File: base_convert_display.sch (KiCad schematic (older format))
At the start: 30 parts, among them Q10 Q_PNP_BEC, Q11 Q_PNP_BEC, Q12 Q_PNP_BEC, Q13 Q_PNP_BEC, Q14 Q_PNP_BEC, Q15 Q_PNP_BEC, Q16 Q_PNP_BEC, Q17 Q_PNP_BEC, Q18 Q_PNP_BEC, Q19 Q_PNP_BEC, Q20 Q_NPN_BEC, Q21 Q_NPN_BEC, Q22 Q_NPN_BEC, Q23 Q_NPN_BEC, Q24 Q_NPN_BEC, Q25 Q_NPN_BEC, Q26 Q_NPN_BEC, Q27 Q_NPN_BEC

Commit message: update RN part numbers
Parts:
- RN10, RN4, RN5, RN6, RN9: Description RES ARRAY 4 RES 4.7K OHM 1206 -> RES ARRAY 4 RES 5.6K OHM 2012; Manufacture Stackpole Electronics Inc. -> Rohm Semiconductor; Mfg Part Number RAVF164DJT4K70 -> MNR34J5ABJ562; Package 1206 -> 2012
- RN7, RN8: Mfg Part Number MNR14ERAPJ151 -> MNR34J5ABJ151; Package 1206 -> 2012
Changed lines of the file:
@@
 F 2 "Resistors_SMD:R_Array_Convex_4x1206" V 1425 1150 50  0001 C CNN
 F 3 "https://www.seielect.com/Catalog/SEI-RAVF.pdf" H 1150 1150 50  0001 C CNN
-F 4 "Stackpole Electronics Inc." H 1150 1150 60  0001 C CNN "Manufacture"
-F 5 "RAVF164DJT4K70" H 1150 1150 60  0001 C CNN "Mfg Part Number"
-F 6 "1206" H 1150 1150 60  0001 C CNN "Package"
-F 7 "RES ARRAY 4 RES 4.7K OHM 1206" H 1150 1150 60  0001 C CNN "Description"
+F 4 "Rohm Semiconductor" H 1150 1150 60  0001 C CNN "Manufacture"
+F 5 "MNR34J5ABJ562" H 1150 1150 60  0001 C CNN "Mfg Part Number"
+F 6 "2012" H 1150 1150 60  0001 C CNN "Package"
+F 7 "RES ARRAY 4 RES 5.6K OHM 2012" H 1150 1150 60  0001 C CNN "Description"
 	1    1150 1150
 	0    1    1    0
@@
 F 3 "http://rohmfs.rohm.com/en/products/databook/datasheet/passive/resistor/chip_resistor_network/mnr_g.pdf" H 8200 1000 50  0001 C CNN
 F 4 "Rohm Semiconductor" H 8200 1000 60  0001 C CNN "Manufacture"
-F 5 "MNR14ERAPJ151" H 8200 1000 60  0001 C CNN "Mfg Part Number"
-F 6 "1206" H 8200 1000 60  0001 C CNN "Package"
+F 5 "MNR34J5ABJ151" H 8200 1000 60  0001 C CNN "Mfg Part Number"
+F 6 "2012" H 8200 1000 60  0001 C CNN "Package"
 F 7 "RES ARRAY 4 RES 150 OHM 1206" H 8200 1000 60  0001 C CNN "Description"
 	1    8200 1000
@@
 F 2 "Resistors_SMD:R_Array_Convex_4x1206" V 1425 3950 50  0001 C CNN
 F 3 "https://www.seielect.com/Catalog/SEI-RAVF.pdf" H 1150 3950 50  0001 C CNN
-F 4 "Stackpole Electronics Inc." H 1150 3950 60  0001 C CNN "Manufacture"
-F 5 "RAVF164DJT4K70" H 1150 3950 60  0001 C CNN "Mfg Part Number"
-F 6 "1206" H 1150 3950 60  0001 C CNN "Package"
-F 7 "RES ARRAY 4 RES 4.7K OHM 1206" H 1150 3950 60  0001 C CNN "Description"
+F 4 "Rohm Semiconductor" H 1150 3950 60  0001 C CNN "Manufacture"
+F 5 "MNR34J5ABJ562" H 1150 3950 60  0001 C CNN "Mfg Part Number"
+F 6 "2012" H 1150 3950 60  0001 C CNN "Package"
+F 7 "RES ARRAY 4 RES 5.6K OHM 2012" H 1150 3950 60  0001 C CNN "Description"
 	1    1150 3950
 	0    1    1    0
@@
 F 2 "Resistors_SMD:R_Array_Convex_4x1206" V 1425 6750 50  0001 C CNN
 F 3 "https://www.seielect.com/Catalog/SEI-RAVF.pdf" H 1150 6750 50  0001 C CNN
-F 4 "Stackpole Electronics Inc." H 1150 6750 60  0001 C CNN "Manufacture"
-F 5 "RAVF164DJT4K70" H 1150 6750 60  0001 C CNN "Mfg Part Number"
-F 6 "1206" H 1150 6750 60  0001 C CNN "Package"
-F 7 "RES ARRAY 4 RES 4.7K OHM 1206" H 1150 6750 60  0001 C CNN "Description"
+F 4 "Rohm Semiconductor" H 1150 6750 60  0001 C CNN "Manufacture"
+F 5 "MNR34J5ABJ562" H 1150 6750 60  0001 C CNN "Mfg Part Number"
+F 6 "2012" H 1150 6750 60  0001 C CNN "Package"
+F 7 "RES ARRAY 4 RES 5.6K OHM 2012" H 1150 6750 60  0001 C CNN "Description"
 	1    1150 6750
 	0    1    1    0
@@
 F 3 "http://rohmfs.rohm.com/en/products/databook/datasheet/passive/resistor/chip_resistor_network/mnr_g.pdf" H 8200 4200 50  0001 C CNN
 F 4 "Rohm Semiconductor" H 8200 4200 60  0001 C CNN "Manufacture"
-F 5 "MNR14ERAPJ151" H 8200 4200 60  0001 C CNN "Mfg Part Number"
-F 6 "1206" H 8200 4200 60  0001 C CNN "Package"
+F 5 "MNR34J5ABJ151" H 8200 4200 60  0001 C CNN "Mfg Part Number"
+F 6 "2012" H 8200 4200 60  0001 C CNN "Package"
 F 7 "RES ARRAY 4 RES 150 OHM 1206" H 8200 4200 60  0001 C CNN "Description"
 	1    8200 4200
@@
 F 2 "Resistors_SMD:R_Array_Convex_4x1206" V 10125 1200 50  0001 C CNN
 F 3 "https://www.seielect.com/Catalog/SEI-RAVF.pdf" H 9850 1200 50  0001 C CNN
-F 4 "Stackpole Electronics Inc." H 9850 1200 60  0001 C CNN "Manufacture"
-F 5 "RAVF164DJT4K70" H 9850 1200 60  0001 C CNN "Mfg Part Number"
-F 6 "1206" H 9850 1200 60  0001 C CNN "Package"
-F 7 "RES ARRAY 4 RES 4.7K OHM 1206" H 9850 1200 60  0001 C CNN "Description"
+F 4 "Rohm Semiconductor" H 9850 1200 60  0001 C CNN "Manufacture"
+F 5 "MNR34J5ABJ562" H 9850 1200 60  0001 C CNN "Mfg Part Number"
+F 6 "2012" H 9850 1200 60  0001 C CNN "Package"
+F 7 "RES ARRAY 4 RES 5.6K OHM 2012" H 9850 1200 60  0001 C CNN "Description"
 	1    9850 1200
 	0    1    1    0
@@
 F 2 "Resistors_SMD:R_Array_Convex_4x1206" V 10125 4400 50  0001 C CNN
 F 3 "https://www.seielect.com/Catalog/SEI-RAVF.pdf" H 9850 4400 50  0001 C CNN
-F 4 "Stackpole Electronics Inc." H 9850 4400 60  0001 C CNN "Manufacture"
-F 5 "RAVF164DJT4K70" H 9850 4400 60  0001 C CNN "Mfg Part Number"
-F 6 "1206" H 9850 4400 60  0001 C CNN "Package"
-F 7 "RES ARRAY 4 RES 4.7K OHM 1206" H 9850 4400 60  0001 C CNN "Description"
+F 4 "Rohm Semiconductor" H 9850 4400 60  0001 C CNN "Manufacture"
+F 5 "MNR34J5ABJ562" H 9850 4400 60  0001 C CNN "Mfg Part Number"
+F 6 "2012" H 9850 4400 60  0001 C CNN "Package"
+F 7 "RES ARRAY 4 RES 5.6K OHM 2012" H 9850 4400 60  0001 C CNN "Description"
 	1    9850 4400
 	0    1    1    0

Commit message: PNP transistor change to prebiased PNP
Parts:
- Q10, Q13: Description TRANS PNP 40V 0.2A SOT25 -> TRANS PREBIAS PNP 250MW TO236AB; Mfg Part Number PMBT3906,235 -> PDTA123ET,215
- Q11, Q18, Q19: Description TRANS PNP 40V 0.2A SOT23 -> TRANS PREBIAS PNP 250MW TO236AB; Mfg Part Number PMBT3906,235 -> PDTA123ET,215
- Q12: Description TRANS PNP 40V 0.2A SOT24 -> TRANS PREBIAS PNP 250MW TO236AB; Mfg Part Number PMBT3906,235 -> PDTA123ET,215
- Q14: Description TRANS PNP 40V 0.2A SOT26 -> TRANS PREBIAS PNP 250MW TO236AB; Mfg Part Number PMBT3906,235 -> PDTA123ET,215
- Q15: Description TRANS PNP 40V 0.2A SOT27 -> TRANS PREBIAS PNP 250MW TO236AB; Mfg Part Number PMBT3906,235 -> PDTA123ET,215
- Q16: Description TRANS PNP 40V 0.2A SOT28 -> TRANS PREBIAS PNP 250MW TO236AB; Mfg Part Number PMBT3906,235 -> PDTA123ET,215
- Q17: Description TRANS PNP 40V 0.2A SOT29 -> TRANS PREBIAS PNP 250MW TO236AB; Mfg Part Number PMBT3906,235 -> PDTA123ET,215
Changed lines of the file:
@@
 F 1 "Q_PNP_BEC" H 1950 900 50  0000 L CNN
 F 2 "TO_SOT_Packages_SMD:SOT-23" H 1950 1050 50  0001 C CNN
-F 3 "https://assets.nexperia.com/documents/data-sheet/PMBT3906.pdf" H 1750 950 50  0001 C CNN
-F 4 "TRANS PNP 40V 0.2A SOT25" H 1950 1100 50  0001 C CNN "Description"
+F 3 "https://assets.nexperia.com/documents/data-sheet/PDTA123E_SERIES.pdf" H 1750 950 50  0001 C CNN
+F 4 "TRANS PREBIAS PNP 250MW TO236AB" H 1950 1100 50  0001 C CNN "Description"
 F 5 "Nexperia USA Inc." H 1950 1100 50  0001 C CNN "Manufacture"
-F 6 "PMBT3906,235" H 1950 1100 50  0001 C CNN "Mfg Part Number"
+F 6 "PDTA123ET,215" H 1950 1100 50  0001 C CNN "Mfg Part Number"
 F 7 "SOT-23" H 1950 1100 50  0001 C CNN "Package"
 	1    1750 950
@@
 F 1 "Q_PNP_BEC" H 1950 1600 50  0000 L CNN
 F 2 "TO_SOT_Packages_SMD:SOT-23" H 1950 1750 50  0001 C CNN
-F 3 "https://assets.nexperia.com/documents/data-sheet/PMBT3906.pdf" H 1750 1650 50  0001 C CNN
-F 4 "TRANS PNP 40V 0.2A SOT23" H 1950 1800 50  0001 C CNN "Description"
+F 3 "https://assets.nexperia.com/documents/data-sheet/PDTA123E_SERIES.pdf" H 1750 1650 50  0001 C CNN
+F 4 "TRANS PREBIAS PNP 250MW TO236AB" H 1950 1800 50  0001 C CNN "Description"
 F 5 "Nexperia USA Inc." H 1950 1800 50  0001 C CNN "Manufacture"
-F 6 "PMBT3906,235" H 1950 1800 50  0001 C CNN "Mfg Part Number"
+F 6 "PDTA123ET,215" H 1950 1800 50  0001 C CNN "Mfg Part Number"
 F 7 "SOT-23" H 1950 1800 50  0001 C CNN "Package"
 	1    1750 1650
@@
 F 1 "Q_PNP_BEC" H 1950 2300 50  0000 L CNN
 F 2 "TO_SOT_Packages_SMD:SOT-23" H 1950 2450 50  0001 C CNN
-F 3 "https://assets.nexperia.com/documents/data-sheet/PMBT3906.pdf" H 1750 2350 50  0001 C CNN
-F 4 "TRANS PNP 40V 0.2A SOT24" H 1950 2500 50  0001 C CNN "Description"
+F 3 "https://assets.nexperia.com/documents/data-sheet/PDTA123E_SERIES.pdf" H 1750 2350 50  0001 C CNN
+F 4 "TRANS PREBIAS PNP 250MW TO236AB" H 1950 2500 50  0001 C CNN "Description"
 F 5 "Nexperia USA Inc." H 1950 2500 50  0001 C CNN "Manufacture"
-F 6 "PMBT3906,235" H 1950 2500 50  0001 C CNN "Mfg Part Number"
+F 6 "PDTA123ET,215" H 1950 2500 50  0001 C CNN "Mfg Part Number"
 F 7 "SOT-23" H 1950 2500 50  0001 C CNN "Package"
 	1    1750 2350
@@
 F 1 "Q_PNP_BEC" H 1950 3000 50  0000 L CNN
 F 2 "TO_SOT_Packages_SMD:SOT-23" H 1950 3150 50  0001 C CNN
-F 3 "https://assets.nexperia.com/documents/data-sheet/PMBT3906.pdf" H 1750 3050 50  0001 C CNN
-F 4 "TRANS PNP 40V 0.2A SOT25" H 1950 3200 50  0001 C CNN "Description"
+F 3 "https://assets.nexperia.com/documents/data-sheet/PDTA123E_SERIES.pdf" H 1750 3050 50  0001 C CNN
+F 4 "TRANS PREBIAS PNP 250MW TO236AB" H 1950 3200 50  0001 C CNN "Description"
 F 5 "Nexperia USA Inc." H 1950 3200 50  0001 C CNN "Manufacture"
-F 6 "PMBT3906,235" H 1950 3200 50  0001 C CNN "Mfg Part Number"
+F 6 "PDTA123ET,215" H 1950 3200 50  0001 C CNN "Mfg Part Number"
 F 7 "SOT-23" H 1950 3200 50  0001 C CNN "Package"
 	1    1750 3050
@@
 F 1 "Q_PNP_BEC" H 1950 3700 50  0000 L CNN
 F 2 "TO_SOT_Packages_SMD:SOT-23" H 1950 3850 50  0001 C CNN
-F 3 "https://assets.nexperia.com/documents/data-sheet/PMBT3906.pdf" H 1750 3750 50  0001 C CNN
-F 4 "TRANS PNP 40V 0.2A SOT26" H 1950 3900 50  0001 C CNN "Description"
+F 3 "https://assets.nexperia.com/documents/data-sheet/PDTA123E_SERIES.pdf" H 1750 3750 50  0001 C CNN
+F 4 "TRANS PREBIAS PNP 250MW TO236AB" H 1950 3900 50  0001 C CNN "Description"
 F 5 "Nexperia USA Inc." H 1950 3900 50  0001 C CNN "Manufacture"
-F 6 "PMBT3906,235" H 1950 3900 50  0001 C CNN "Mfg Part Number"
+F 6 "PDTA123ET,215" H 1950 3900 50  0001 C CNN "Mfg Part Number"
 F 7 "SOT-23" H 1950 3900 50  0001 C CNN "Package"
 	1    1750 3750
@@
 F 1 "Q_PNP_BEC" H 1950 4400 50  0000 L CNN
 F 2 "TO_SOT_Packages_SMD:SOT-23" H 1950 4550 50  0001 C CNN
-F 3 "https://assets.nexperia.com/documents/data-sheet/PMBT3906.pdf" H 1750 4450 50  0001 C CNN
-F 4 "TRANS PNP 40V 0.2A SOT27" H 1950 4600 50  0001 C CNN "Description"
+F 3 "https://assets.nexperia.com/documents/data-sheet/PDTA123E_SERIES.pdf" H 1750 4450 50  0001 C CNN
+F 4 "TRANS PREBIAS PNP 250MW TO236AB" H 1950 4600 50  0001 C CNN "Description"
 F 5 "Nexperia USA Inc." H 1950 4600 50  0001 C CNN "Manufacture"
-F 6 "PMBT3906,235" H 1950 4600 50  0001 C CNN "Mfg Part Number"
+F 6 "PDTA123ET,215" H 1950 4600 50  0001 C CNN "Mfg Part Number"
 F 7 "SOT-23" H 1950 4600 50  0001 C CNN "Package"
 	1    1750 4450
@@
 F 1 "Q_PNP_BEC" H 1950 5100 50  0000 L CNN
 F 2 "TO_SOT_Packages_SMD:SOT-23" H 1950 5250 50  0001 C CNN
-F 3 "https://assets.nexperia.com/documents/data-sheet/PMBT3906.pdf" H 1750 5150 50  0001 C CNN
-F 4 "TRANS PNP 40V 0.2A SOT28" H 1950 5300 50  0001 C CNN "Description"
+F 3 "https://assets.nexperia.com/documents/data-sheet/PDTA123E_SERIES.pdf" H 1750 5150 50  0001 C CNN
+F 4 "TRANS PREBIAS PNP 250MW TO236AB" H 1950 5300 50  0001 C CNN "Description"
 F 5 "Nexperia USA Inc." H 1950 5300 50  0001 C CNN "Manufacture"
-F 6 "PMBT3906,235" H 1950 5300 50  0001 C CNN "Mfg Part Number"
+F 6 "PDTA123ET,215" H 1950 5300 50  0001 C CNN "Mfg Part Number"
 F 7 "SOT-23" H 1950 5300 50  0001 C CNN "Package"
 	1    1750 5150
@@
 F 1 "Q_PNP_BEC" H 1950 5800 50  0000 L CNN
 F 2 "TO_SOT_Packages_SMD:SOT-23" H 1950 5950 50  0001 C CNN
-F 3 "https://assets.nexperia.com/documents/data-sheet/PMBT3906.pdf" H 1750 5850 50  0001 C CNN
-F 4 "TRANS PNP 40V 0.2A SOT29" H 1950 6000 50  0001 C CNN "Description"
+F 3 "https://assets.nexperia.com/documents/data-sheet/PDTA123E_SERIES.pdf" H 1750 5850 50  0001 C CNN
+F 4 "TRANS PREBIAS PNP 250MW TO236AB" H 1950 6000 50  0001 C CNN "Description"
 F 5 "Nexperia USA Inc." H 1950 6000 50  0001 C CNN "Manufacture"
-F 6 "PMBT3906,235" H 1950 6000 50  0001 C CNN "Mfg Part Number"
+F 6 "PDTA123ET,215" H 1950 6000 50  0001 C CNN "Mfg Part Number"
 F 7 "SOT-23" H 1950 6000 50  0001 C CNN "Package"
 	1    1750 5850
@@
 F 1 "Q_PNP_BEC" H 1950 6500 50  0000 L CNN
 F 2 "TO_SOT_Packages_SMD:SOT-23" H 1950 6650 50  0001 C CNN
-F 3 "https://assets.nexperia.com/documents/data-sheet/PMBT3906.pdf" H 1750 6550 50  0001 C CNN
-F 4 "TRANS PNP 40V 0.2A SOT23" H 1950 6700 50  0001 C CNN "Description"
+F 3 "https://assets.nexperia.com/documents/data-sheet/PDTA123E_SERIES.pdf" H 1750 6550 50  0001 C CNN
+F 4 "TRANS PREBIAS PNP 250MW TO236AB" H 1950 6700 50  0001 C CNN "Description"
 F 5 "Nexperia USA Inc." H 1950 6700 50  0001 C CNN "Manufacture"
-F 6 "PMBT3906,235" H 1950 6700 50  0001 C CNN "Mfg Part Number"
+F 6 "PDTA123ET,215" H 1950 6700 50  0001 C CNN "Mfg Part Number"
 F 7 "SOT-23" H 1950 6700 50  0001 C CNN "Package"
 	1    1750 6550
@@
 F 1 "Q_PNP_BEC" H 1950 7200 50  0000 L CNN
 F 2 "TO_SOT_Packages_SMD:SOT-23" H 1950 7350 50  0001 C CNN
-F 3 "https://assets.nexperia.com/documents/data-sheet/PMBT3906.pdf" H 1750 7250 50  0001 C CNN
-F 4 "TRANS PNP 40V 0.2A SOT23" H 1950 7400 50  0001 C CNN "Description"
+F 3 "https://assets.nexperia.com/documents/data-sheet/PDTA123E_SERIES.pdf" H 1750 7250 50  0001 C CNN
+F 4 "TRANS PREBIAS PNP 250MW TO236AB" H 1950 7400 50  0001 C CNN "Description"
 F 5 "Nexperia USA Inc." H 1950 7400 50  0001 C CNN "Manufacture"
-F 6 "PMBT3906,235" H 1950 7400 50  0001 C CNN "Mfg Part Number"
+F 6 "PDTA123ET,215" H 1950 7400 50  0001 C CNN "Mfg Part Number"
 F 7 "SOT-23" H 1950 7400 50  0001 C CNN "Package"
 	1    1750 7250

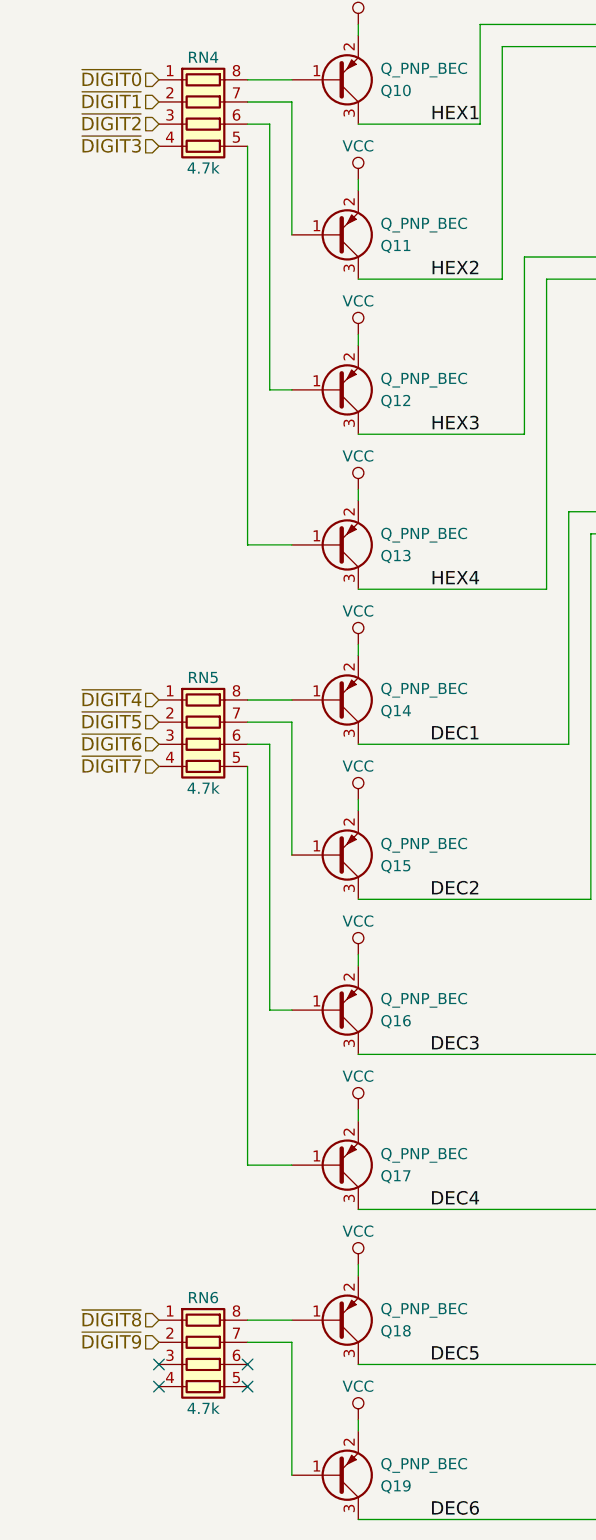
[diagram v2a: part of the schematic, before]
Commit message: PNP base resistor network change to 10k
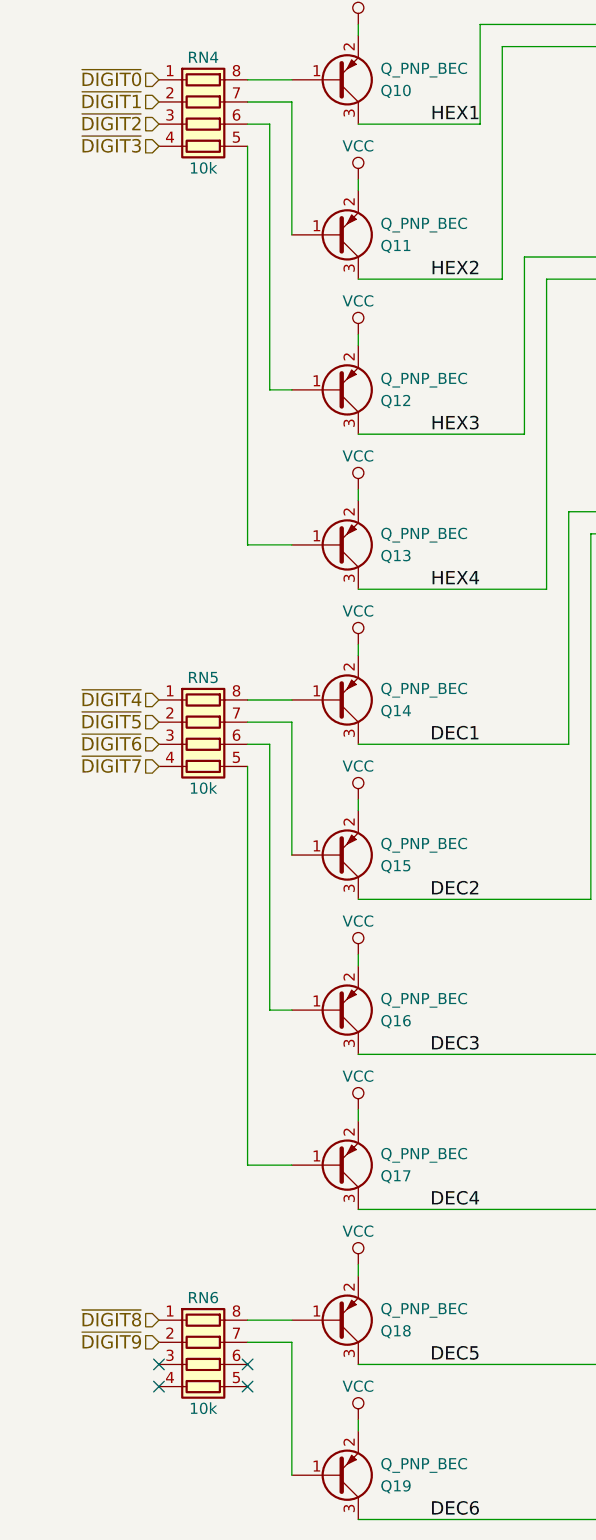
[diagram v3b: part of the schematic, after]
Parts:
- RN4, RN5, RN6: value 4.7k -> 10k; Description RES ARRAY 4 RES 5.6K OHM 2012 -> RES ARRAY 4 RES 10K OHM 2012; Manufacture Rohm Semiconductor -> Yageo; Mfg Part Number MNR34J5ABJ562 -> YC324-JK-0710KL
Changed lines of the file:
@@
 P 1150 1150
 F 0 "RN4" V 850 1150 50  0000 C CNN
-F 1 "4.7k" V 1350 1150 50  0000 C CNN
+F 1 "10k" V 1350 1150 50  0000 C CNN
 F 2 "Resistors_SMD:R_Array_Convex_4x1206" V 1425 1150 50  0001 C CNN
-F 3 "https://www.seielect.com/Catalog/SEI-RAVF.pdf" H 1150 1150 50  0001 C CNN
-F 4 "Rohm Semiconductor" H 1150 1150 60  0001 C CNN "Manufacture"
-F 5 "MNR34J5ABJ562" H 1150 1150 60  0001 C CNN "Mfg Part Number"
+F 3 "https://media.digikey.com/pdf/Data%20Sheets/Yageo%20PDFs/YC102-358,TC122-164_Series_DS.pdf" H 1150 1150 50  0001 C CNN
+F 4 "Yageo" H 1150 1150 60  0001 C CNN "Manufacture"
+F 5 "YC324-JK-0710KL" H 1150 1150 60  0001 C CNN "Mfg Part Number"
 F 6 "2012" H 1150 1150 60  0001 C CNN "Package"
-F 7 "RES ARRAY 4 RES 5.6K OHM 2012" H 1150 1150 60  0001 C CNN "Description"
+F 7 "RES ARRAY 4 RES 10K OHM 2012" H 1150 1150 60  0001 C CNN "Description"
 	1    1150 1150
 	0    1    1    0
@@
 P 1150 3950
 F 0 "RN5" V 850 3950 50  0000 C CNN
-F 1 "4.7k" V 1350 3950 50  0000 C CNN
+F 1 "10k" V 1350 3950 50  0000 C CNN
 F 2 "Resistors_SMD:R_Array_Convex_4x1206" V 1425 3950 50  0001 C CNN
-F 3 "https://www.seielect.com/Catalog/SEI-RAVF.pdf" H 1150 3950 50  0001 C CNN
-F 4 "Rohm Semiconductor" H 1150 3950 60  0001 C CNN "Manufacture"
-F 5 "MNR34J5ABJ562" H 1150 3950 60  0001 C CNN "Mfg Part Number"
+F 3 "https://media.digikey.com/pdf/Data%20Sheets/Yageo%20PDFs/YC102-358,TC122-164_Series_DS.pdf" H 1150 3950 50  0001 C CNN
+F 4 "Yageo" H 1150 3950 60  0001 C CNN "Manufacture"
+F 5 "YC324-JK-0710KL" H 1150 3950 60  0001 C CNN "Mfg Part Number"
 F 6 "2012" H 1150 3950 60  0001 C CNN "Package"
-F 7 "RES ARRAY 4 RES 5.6K OHM 2012" H 1150 3950 60  0001 C CNN "Description"
+F 7 "RES ARRAY 4 RES 10K OHM 2012" H 1150 3950 60  0001 C CNN "Description"
 	1    1150 3950
 	0    1    1    0
@@
 P 1150 6750
 F 0 "RN6" V 850 6750 50  0000 C CNN
-F 1 "4.7k" V 1350 6750 50  0000 C CNN
+F 1 "10k" V 1350 6750 50  0000 C CNN
 F 2 "Resistors_SMD:R_Array_Convex_4x1206" V 1425 6750 50  0001 C CNN
-F 3 "https://www.seielect.com/Catalog/SEI-RAVF.pdf" H 1150 6750 50  0001 C CNN
-F 4 "Rohm Semiconductor" H 1150 6750 60  0001 C CNN "Manufacture"
-F 5 "MNR34J5ABJ562" H 1150 6750 60  0001 C CNN "Mfg Part Number"
+F 3 "https://media.digikey.com/pdf/Data%20Sheets/Yageo%20PDFs/YC102-358,TC122-164_Series_DS.pdf" H 1150 6750 50  0001 C CNN
+F 4 "Yageo" H 1150 6750 60  0001 C CNN "Manufacture"
+F 5 "YC324-JK-0710KL" H 1150 6750 60  0001 C CNN "Mfg Part Number"
 F 6 "2012" H 1150 6750 60  0001 C CNN "Package"
-F 7 "RES ARRAY 4 RES 5.6K OHM 2012" H 1150 6750 60  0001 C CNN "Description"
+F 7 "RES ARRAY 4 RES 10K OHM 2012" H 1150 6750 60  0001 C CNN "Description"
 	1    1150 6750
 	0    1    1    0
